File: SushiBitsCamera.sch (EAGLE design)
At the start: 1 part, among them IC1 V3SH

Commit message: Finished: CPU Power section
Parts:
- added C1, C12, C14, C15, C16, C18, C2, C20, C21, C22, C23, C24, C25, C26, C27, C9: 100n, rcl:C-EUC0603
- added C10, C11, C13, C17, C19, C8: 10u, rcl:C-EUC0603
- added C3: 4.7u, rcl:C-EUC0603
- added C4, C5: 22p, rcl:C-EUC0603
- added C6, C7: 6p, rcl:C-EUC0603
- added IC2: LM3671MF-1.8, ARM926SBC:LM3671MF-1.8
- added L1: 4.7u, rcl:L-EUL5650M
- added R1, R2: 1k, rcl:R-EU_R0603
- added R3: 240, rcl:R-EU_R0603
- added Y1: 32768, SparkFun-FreqCtrl:CRYSTAL3.2X1.5MM
- added Y2: 24M, SparkFun-FreqCtrl:CRYSTALCRYSTAL-SMD-5X3-16MHZ
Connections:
- new net !RESET: IC1-POWER.!RESET
- new net AVDD: C27.1, IC1-POWER.AVCC, IC1-POWER.VDDPLL
- new net GND: C1.2, C10.2, C11.2, C12.2, C13.2, C14.2, C15.2, C16.2, C17.2, C18.2, C19.2, C2.2, C20.2, C21.2, C22.2, C23.2, C24.2, C25.2, C26.2, C27.2, C3.2, C4.2, C5.2, C6.2, C7.2, C8.2, C9.2, IC1-POWER.AGND, IC1-POWER.GND, IC2.GND, R2.1, R3.1
- new net N$1: C2.1, IC1-POWER.AVDDPO
- new net N$2: IC1-POWER.SZQ, R3.2
- new net N$3: C4.1, IC1-POWER.XI, Y2.1
- new net N$4: C5.1, IC1-POWER.XO, Y2.2
- new net N$5: C6.1, IC1-POWER.RTCI, Y1.1
- new net N$6: C7.1, IC1-POWER.RTCO, Y1.2
- new net N$7: C3.1, IC1-POWER.RTCVIO
- new net N$8: IC2.SW, L1.2
- new net SVREF: C1.1, IC1-POWER.SVREF, R1.1, R2.2
- new net VBACKUP: C26.1, IC1-POWER.VBACKUP
- new net VCC: C10.1, C17.1, C18.1, C19.1, C20.1, C21.1, C22.1, C23.1, C24.1, C25.1, IC1-POWER.AVDDP, IC1-POWER.VCCETH, IC1-POWER.VDDCSI, IC1-POWER.VDDIO, IC1-POWER.VDDIOE, IC1-POWER.VDDUSB, IC2.CE, IC2.VIN
- new net VCORE: C11.1, C12.1, C13.1, C14.1, C15.1, C16.1, IC1-POWER.VCORE, IC1-POWER.VDDETH, IC1-POWER.VDDSYS
- new net VDDRAM: C8.1, C9.1, IC1-POWER.VDDRAM, IC2.FB, L1.1, R1.2
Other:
- note added: "CPU Power"
- note added: "Copyright (c) 2017 Max Chan <xcvista@me.com> Open Source Hardware under the 3-clause BSD License"

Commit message: Implementing components for SMPS
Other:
- note added: "System Power"
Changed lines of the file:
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@@
 <part name="GND8" library="supply1" deviceset="GND" device=""/>
 <part name="P+3" library="supply1" deviceset="VCC" device=""/>
+<part name="FRAME2" library="frames" deviceset="A4L-LOC" device=""/>
 </parts>
 <sheets>
 <sheet>
 <plain>
+<text x="217.17" y="20.32" size="2.54" layer="94">System Power</text>
+<text x="5.08" y="5.08" size="2.54" layer="94">Copyright (c) 2017 Max Chan &lt;xcvista@me.com&gt;
+Open Source Hardware under the 3-clause BSD License</text>
 </plain>
 <instances>
+<instance part="FRAME2" gate="G$1" x="0" y="0"/>
 </instances>
 <busses>

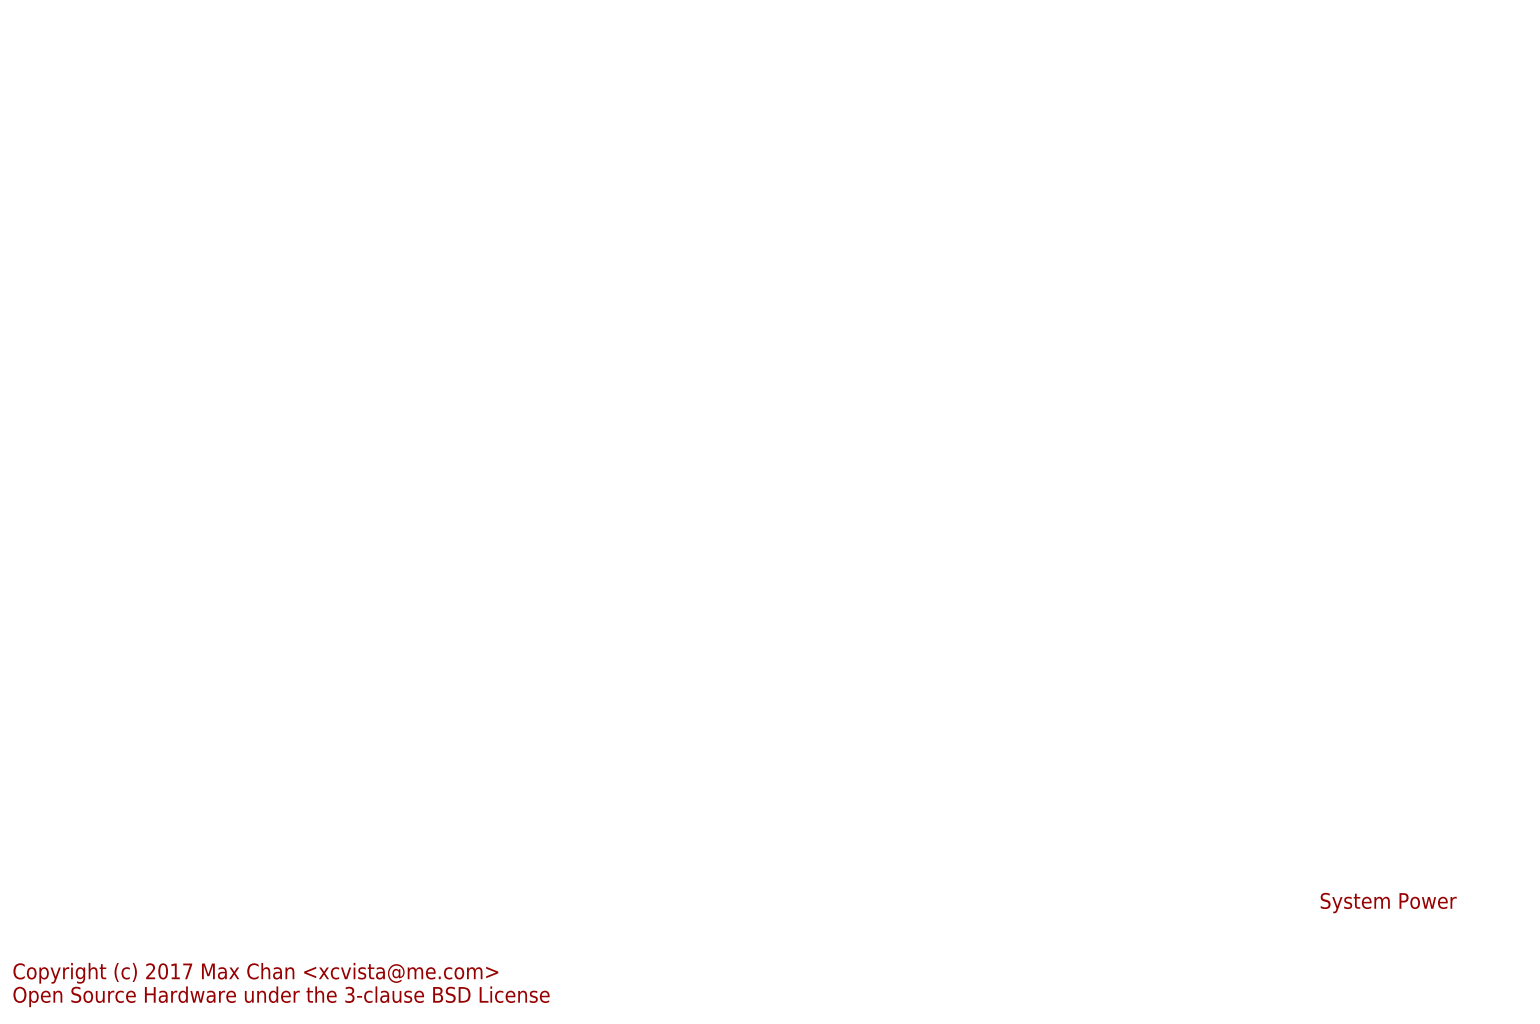
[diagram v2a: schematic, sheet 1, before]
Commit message: Added some power converter circuitry.Maybe I should switch over to something else?
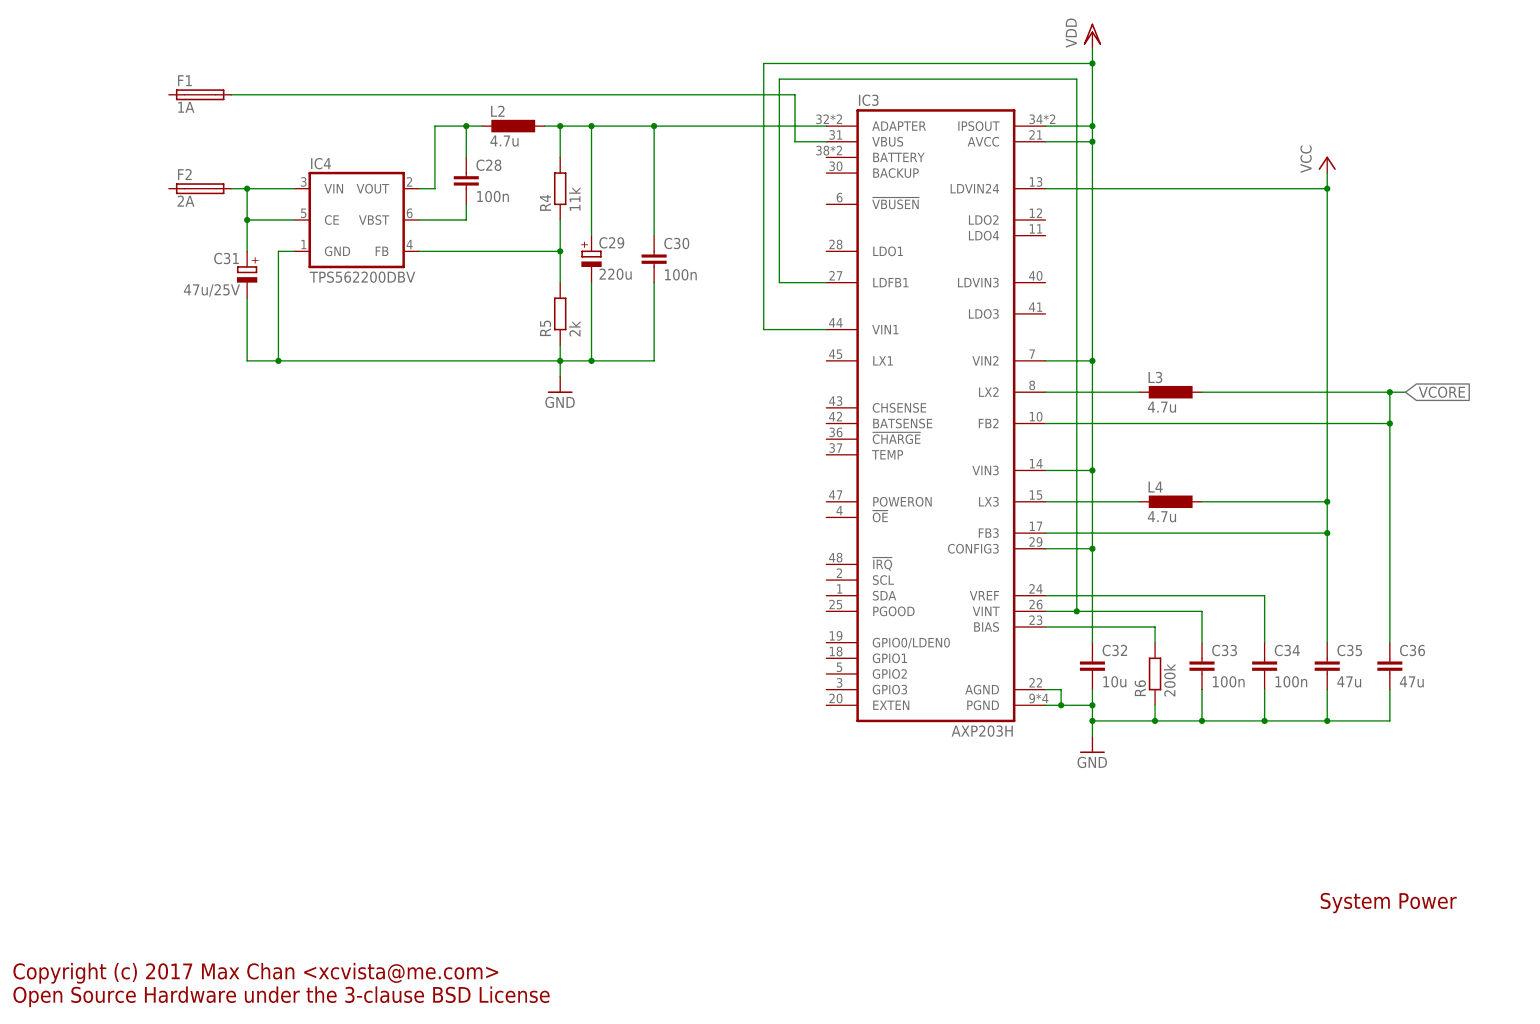
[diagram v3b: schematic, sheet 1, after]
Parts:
- added C28, C30, C33, C34: 100n, rcl:C-EUC0603
- added C29: 220u, rcl:CPOL-EUSMCB
- added C31: 47u/25V, rcl:CPOL-EUSMCD
- added C32: 10u, rcl:C-EUC0603
- added C35, C36: 47u, rcl:C-EUC1206
- added F1: 1A, fuse:FUSER1206
- added F2: 2A, fuse:FUSER1206
- added IC3: AXP203H, AllWinner V3s:AXP203H
- added IC4: TPS562200DBV, AllWinner V3s:TPS562200DBV
- added L2, L3, L4: 4.7u, rcl:L-EUL5650M
- added R4: 11k, rcl:R-EU_R0603
- added R5: 2k, rcl:R-EU_R0603
- added R6: 200k, rcl:R-EU_R0603
- IC2: device ARM926SBC:LM3671MF-1.8 -> AllWinner V3s:LM3671MF-1.8
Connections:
- new net N$10: C29.+, C30.1, IC3.ADAPTER, L2.1, R4.2
- new net N$11: C28.1, IC4.VOUT, L2.2
- new net N$12: C28.2, IC4.VBST
- new net N$13: IC4.FB, R4.1, R5.2
- new net N$14: C31.+, F2.2, IC4.CE, IC4.VIN
- new net N$16: IC3.BIAS, R6.2
- new net N$17: C33.1, IC3.LDFB1, IC3.VINT
- new net N$18: C34.1, IC3.VREF
- new net N$21: IC3.LX2, L3.2
- new net N$22: IC3.LX3, L4.2
- new net N$9: F1.2, IC3.VBUS
- new net VDD: C10.1, C32.1, IC2.CE, IC2.VIN, IC3.AVCC, IC3.CONFIG3, IC3.IPSOUT, IC3.VIN1, IC3.VIN2, IC3.VIN3
- net GND: now also C29.-, C30.2, C31.-, C32.2, C33.2, C34.2, C35.2, C36.2, IC3.AGND, IC3.PGND, IC4.GND, R5.1, R6.1
- net VCC: now also C35.1, IC3.FB3, IC3.LDVIN24, L4.1; no longer C10.1, IC2.CE, IC2.VIN
- net VCORE: now also C36.1, IC3.FB2, L3.1

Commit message: More Power section. Really should move over to things like LM2642...
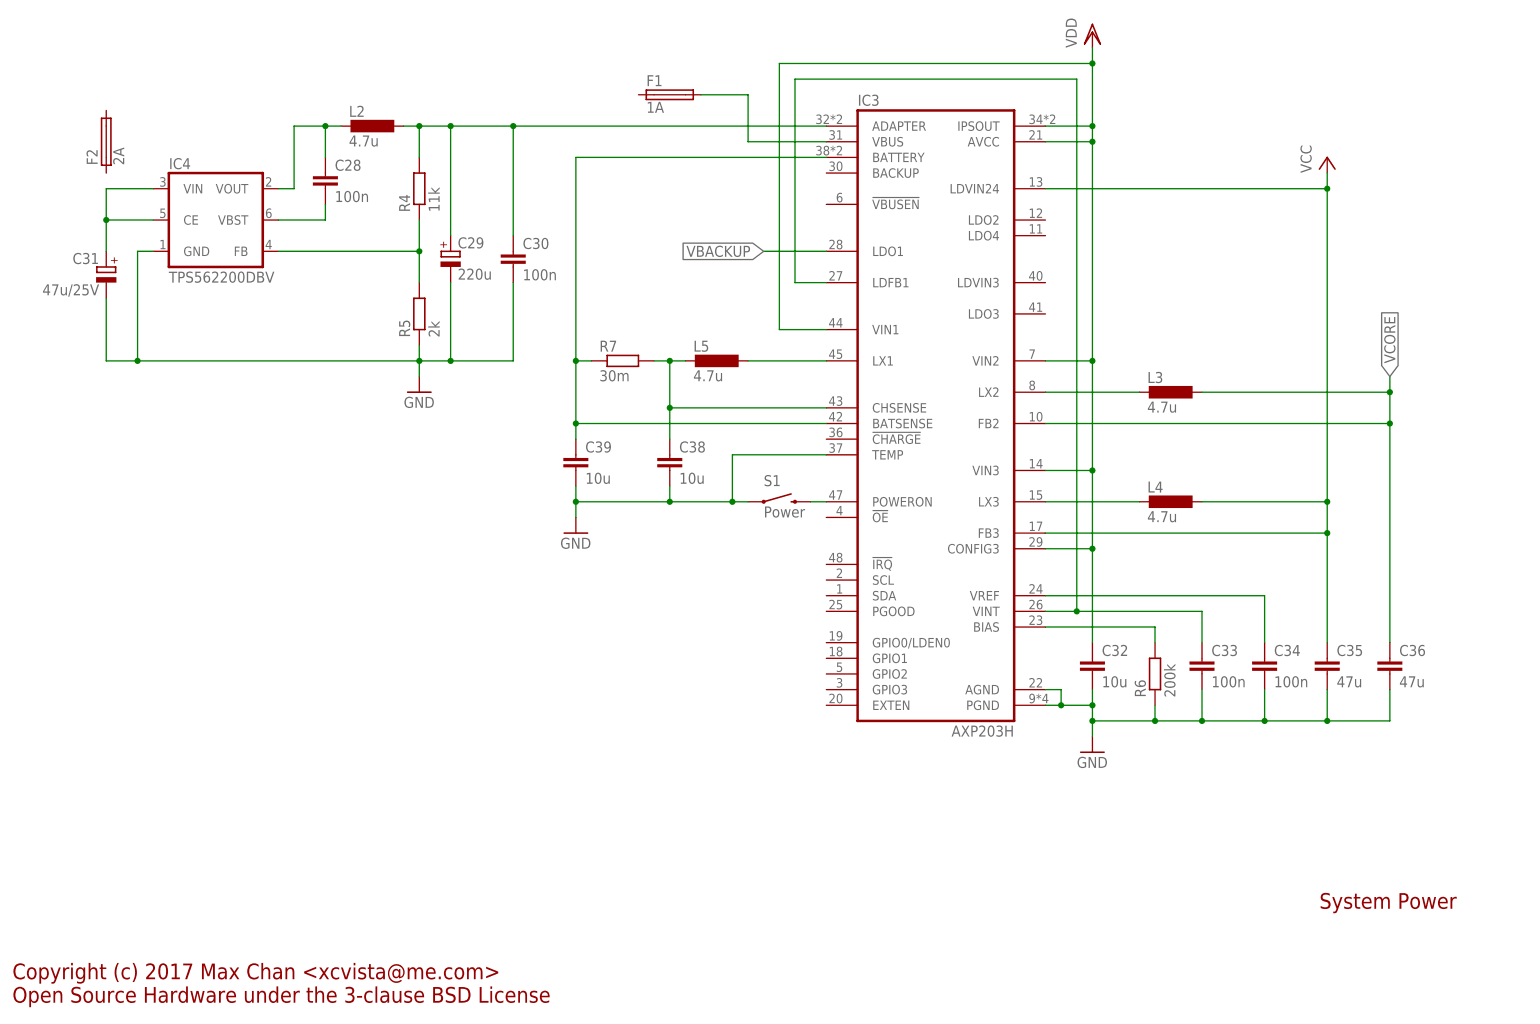
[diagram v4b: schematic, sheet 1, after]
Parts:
- added C37: 100n, rcl:C-EUC0603
- added C38, C39: 10u, rcl:C-EUC0603
- added L5: 4.7u, rcl:L-EUL5650M
- added R7: 30m, rcl:R-EU_R2512
- added S1: Power, SparkFun-Electromechanical:SWITCH-MOMENTARY-2SIDE_EZ
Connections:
- new net N$15: C38.1, IC3.CHSENSE, L5.2, R7.2
- new net N$19: IC3.LX1, L5.1
- new net N$20: C39.1, IC3.BATSENSE, IC3.BATTERY, R7.1
- new net N$23: IC3.POWERON, S1.2
- net GND: now also C37.2, C38.2, C39.2, IC3.TEMP, S1.1
- net N$14: no longer F2.2
- net VBACKUP: now also IC3.LDO1
- net VCC: no longer IC1-POWER.AVDDP
- net VDD: now also C37.1, IC1-POWER.AVDDP
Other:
- moved on the sheet: C1, C10, C26, C27, C28, C29, C30, C31, C8, C9, F1, F2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

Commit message: I think I have a full power stack..?
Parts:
- added C40, C41, C42: 47u, rcl:C-EUC1206
- added D1: SS14, diode:SCHOTTKY-DIODEDO214AC
- added D2: SS34, diode:SCHOTTKY-DIODEDO214AC
- added J1: (no value), con-jack:JACK-PLUG0
- added J2: USD-HOLDER, AllWinner V3s:USD-HOLDER
- added JP1: (no value), pinhead:PINHD-1X2
- added R8: (no value), rcl:R-EU_R0603
- added RESET: Power, SparkFun-Electromechanical:SWITCH-MOMENTARY-2SIDE_EZ
- added RN1: 4.7k, resistor-dil:4R-NEXB38V
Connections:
- new net !IRQ: IC3.!IRQ, RN1B.2
- new net !VBUSEN: IC3.!VBUSEN
- new net N$24: IC3.!OE, RESET.2, RN1A.2
- new net N$25: C40.1, IC3.LDO3
- new net N$26: C41.1, IC3.LDO4
- new net N$27: D2.A, J1.3
- new net N$28: D2.C, F2.2
- new net N$29: IC1-PORTFG.PF5/SD0_D2/TCK, J2.DAT2
- new net N$30: IC3.PGOOD, R8.2
- new net N$31: IC1-PORTFG.PF4/SD0_D3/RX0, J2.CD/DAT3
- new net N$32: IC1-PORTFG.PF3/SD0_CMD/TDO, J2.CMD
- new net N$33: IC1-PORTFG.PF2/SD0_CLK/TX0, J2.CLK
- new net N$34: IC1-PORTFG.PF1/SD0_D0/TDI, J2.DAT0
- new net N$35: IC1-PORTFG.PF0/SD0_D1/TMS, J2.DAT1
- new net SCL: IC3.SCL, RN1C.2
- new net SDA: IC3.SDA, RN1D.2
- new net VBUS: F1.1
- net !RESET: now also R8.1
- net AVDD: now also C42.1, IC3.LDO2
- net GND: now also C40.2, C41.2, C42.2, J1.1, J1.2, J2.GND, J2.SHIELD, JP1.2, RN1A.1
- net N$10: now also D1.A
- net N$14: now also F2.1
- net N$20: now also JP1.1
- net N$9: now also D1.C
- net VCC: now also IC3.LDVIN3, J2.VCC
- net VDD: now also RESET.1, RN1B.1, RN1C.1, RN1D.1
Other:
- note added: "Power rails: VIN: 5-17V, 2A (barrel jack) VBUS: 5V, 1A (USB) VBAT: 4.2V (Li-po) VDD: 4.2V (Switched Li-po) VCC: 3.3V (System Voltage) AVDD: 3.0V (Analog, PLL) VDDR: 1.8V (DRAM) VCORE: 1.2V (ARM core + bus)"
- note added: "SDIO ports"
